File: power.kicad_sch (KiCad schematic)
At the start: 50 parts, among them SW2 SW_DPST, U10 ZLDO1117G33TA

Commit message: prepare for fabrication
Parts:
- C103, C107, C109, C116, C117, C138, C151, C222, C223, C227, C24, C29, C37, C38, C40, C50, C64, C66, C67, C70, C71, C85, C91, C92, C95: LCSC (none) -> C344201; LCSC Part (none) -> C344201
- C20, C21: LCSC C24123 -> C77083; LCSC Part C28323 -> C77083
- TP2, TP3: now not fitted
- U10: LCSC Part (none) -> C18212698

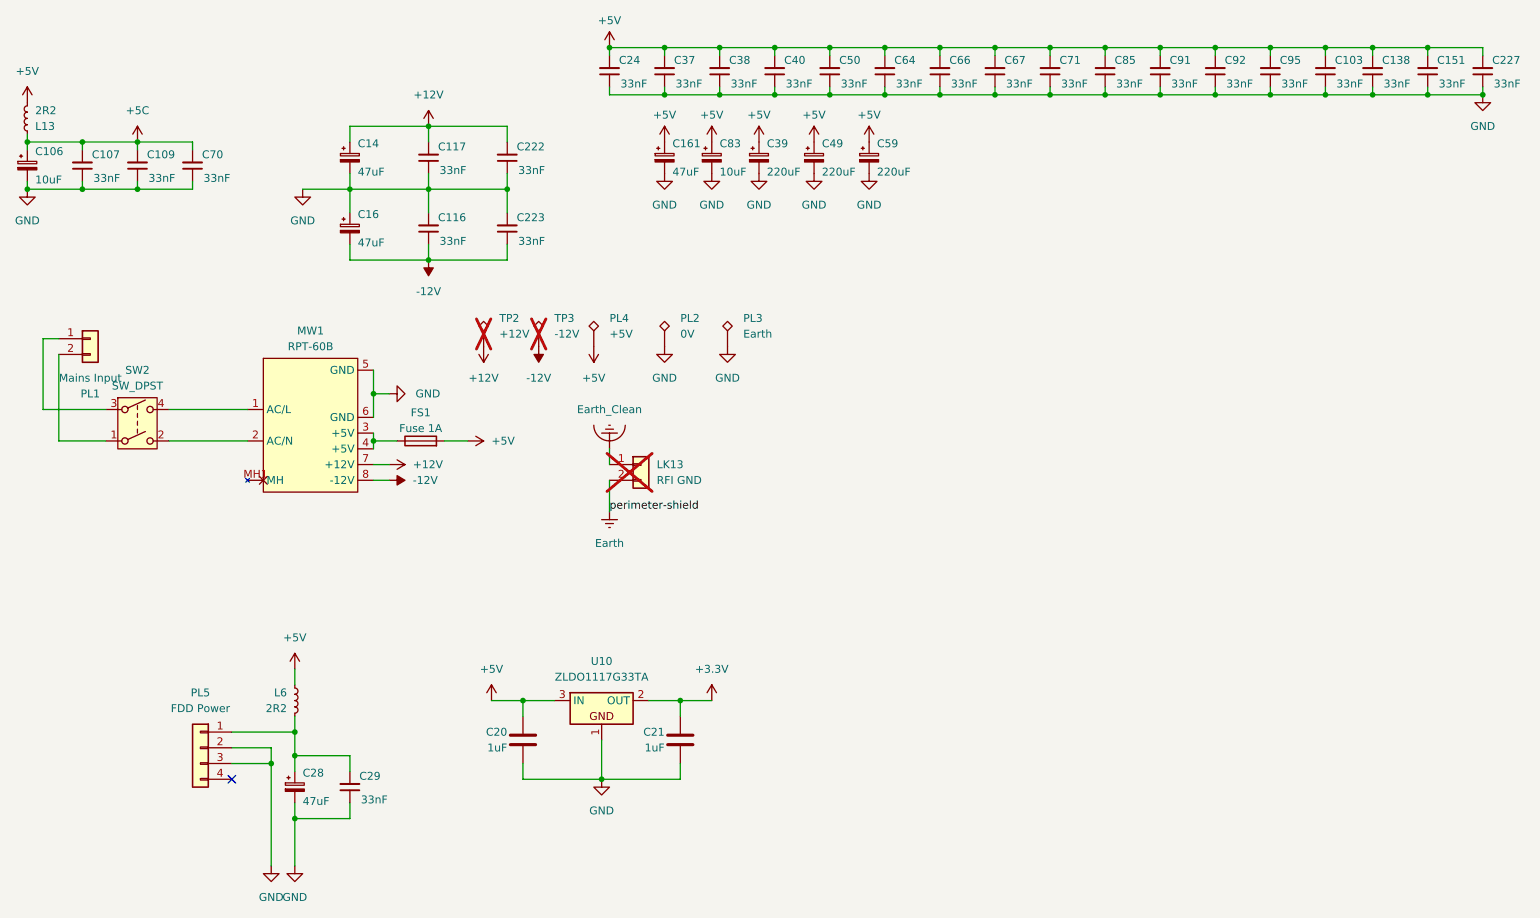
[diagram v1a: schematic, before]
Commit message: verify all component values vs TRM
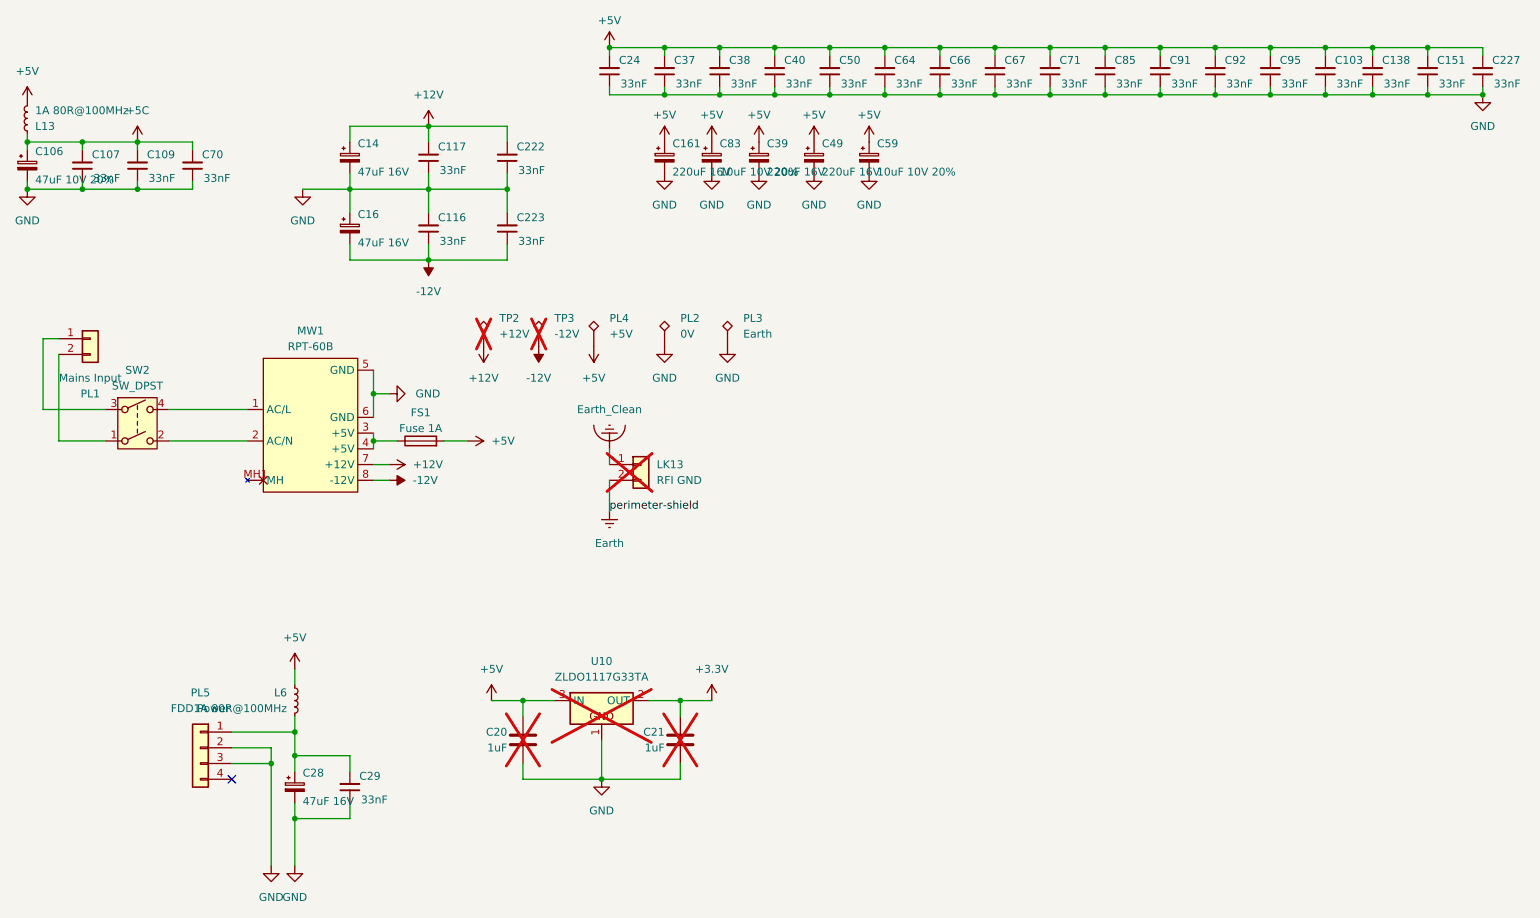
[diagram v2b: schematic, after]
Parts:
- C106: value 10uF -> 47uF 10V 20%
- C14, C16, C28: value 47uF -> 47uF 16V
- C161: value 47uF -> 220uF 16V
- C20, C21, U10: now not fitted; now left out of the parts list
- C39, C49: value 220uF -> 220uF 16V
- C59: value 220uF -> 10uF 10V 20%
- C83: value 10uF -> 10uF 10V 20%
- L13, L6: value 2R2 -> 1A 80R@100MHz
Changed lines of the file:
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@@
 			)
 		)
-		(property "Value" "220uF"
+		(property "Value" "220uF 16V"
 			(at 149.86 41.656 0)
 			(effects
@@
 			)
 		)
-		(property "Value" "47uF"
+		(property "Value" "220uF 16V"
 			(at 134.62 41.656 0)
 			(effects
@@
 			)
 		)
-		(property "Value" "220uF"
+		(property "Value" "10uF 10V 20%"
 			(at 167.64 41.656 0)
 			(effects
@@
 			)
 		)
-		(property "Value" "47uF"
+		(property "Value" "47uF 16V"
 			(at 83.82 41.656 0)
 			(effects
@@
 			)
 		)
-		(property "Value" "10uF"
+		(property "Value" "10uF 10V 20%"
 			(at 142.24 41.656 0)
 			(effects
@@
 		(unit 1)
 		(exclude_from_sim no)
-		(in_bom yes)
+		(in_bom no)
 		(on_board no)
-		(dnp no)
+		(dnp yes)
 		(fields_autoplaced yes)
 		(property "Reference" "U10"
@@
 		(unit 1)
 		(exclude_from_sim no)
-		(in_bom yes)
+		(in_bom no)
 		(on_board no)
-		(dnp no)
+		(dnp yes)
 		(property "Reference" "C21"
 			(at 133.35 132.08 0)
@@
 			)
 		)
-		(property "Value" "10uF"
+		(property "Value" "47uF 10V 20%"
 			(at 31.75 42.926 0)
 			(effects
@@
 		(unit 1)
 		(exclude_from_sim no)
-		(in_bom yes)
+		(in_bom no)
 		(on_board no)
-		(dnp no)
+		(dnp yes)
 		(property "Reference" "C20"
 			(at 107.95 132.08 0)
@@
 			)
 		)
-		(property "Value" "2R2"
+		(property "Value" "1A 80R@100MHz"
 			(at 72.39 128.2699 0)
 			(effects
@@
 			)
 		)
-		(property "Value" "47uF"
+		(property "Value" "47uF 16V"
 			(at 74.93 143.256 0)
 			(effects
@@
 			)
 		)
-		(property "Value" "220uF"
+		(property "Value" "220uF 16V"
 			(at 158.75 41.656 0)
 			(effects
@@
 			)
 		)
-		(property "Value" "2R2"
+		(property "Value" "1A 80R@100MHz"
 			(at 31.75 31.7501 0)
 			(effects
@@
 			)
 		)
-		(property "Value" "47uF"
+		(property "Value" "47uF 16V"
 			(at 83.82 53.086 0)
 			(effects

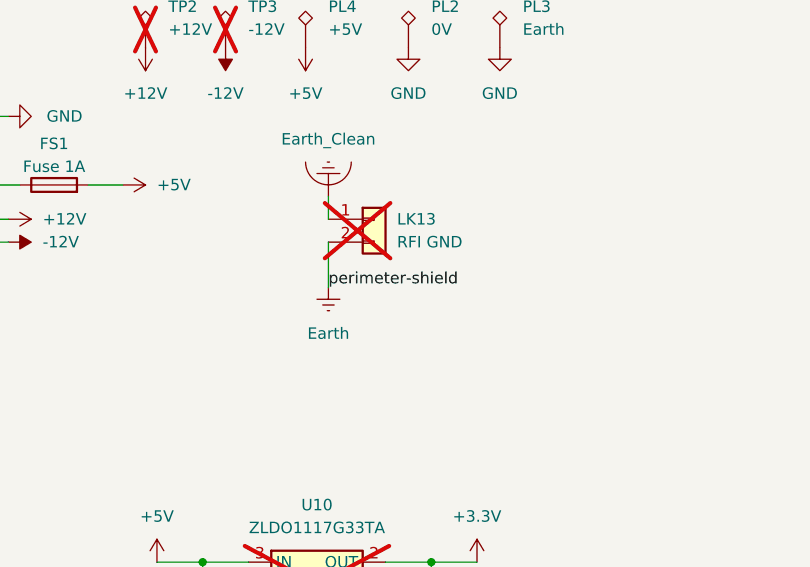
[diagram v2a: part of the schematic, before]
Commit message: switch links to net ties
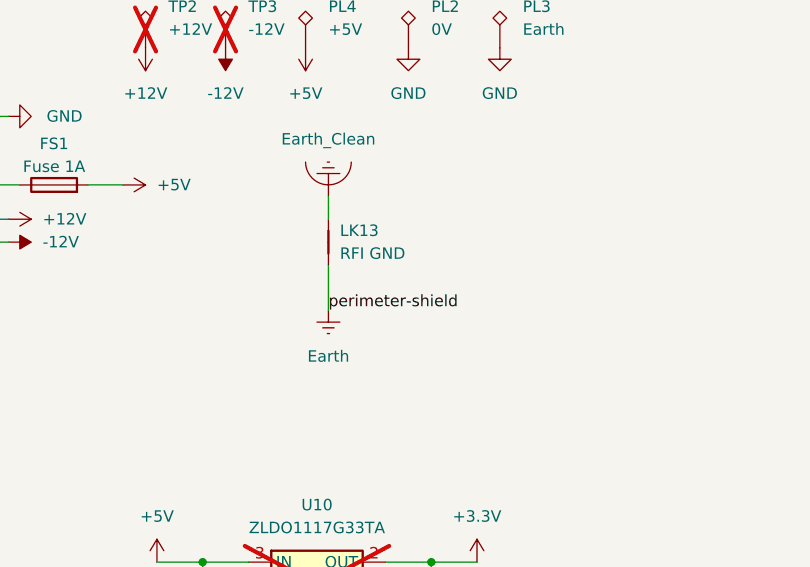
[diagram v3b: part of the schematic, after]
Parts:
- removed LK13: RFI GND, Connector_PinHeader_2.54mm:PinHeader_1x02_P2.54mm_Vertical, symbol Connector_Generic:Conn_01x02
- added LK13: RFI GND, Acorn:Link_Connected, symbol Device:NetTie_2
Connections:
- net Earth: now also LK13.1
- net Earth_Clean: now also LK13.2
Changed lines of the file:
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@@
 	(wire
 		(pts
-			(xy 124.46 91.44) (xy 124.46 96.52)
+			(xy 124.46 93.98) (xy 124.46 99.06)
 		)
 		(stroke
@@
 	)
 	(label "perimeter-shield"
-		(at 124.46 96.52 0)
+		(at 124.46 99.06 0)
 		(effects
 			(font
@@
 	)
 	(symbol
+		(lib_id "Device:NetTie_2")
+		(at 124.46 91.44 90)
+		(unit 1)
+		(exclude_from_sim no)
+		(in_bom no)
+		(on_board yes)
+		(dnp no)
+		(fields_autoplaced yes)
+		(property "Reference" "LK13"
+			(at 125.73 90.1699 90)
+			(effects
+				(font
+					(size 1.27 1.27)
+				)
+				(justify right)
+			)
+		)
+		(property "Value" "RFI GND"
+			(at 125.73 92.7099 90)
+			(effects
+				(font
+					(size 1.27 1.27)
+				)
+				(justify right)
+			)
+		)
+		(property "Footprint" "Acorn:Link_Connected"
+			(at 124.46 91.44 0)
+			(effects
+				(font
+					(size 1.27 1.27)
+				)
+				(hide yes)
+			)
+		)
+		(property "Datasheet" "~"
+			(at 124.46 91.44 0)
+			(effects
+				(font
+					(size 1.27 1.27)
+				)
+				(hide yes)
+			)
+		)
+		(property "Description" "Net tie, 2 pins"
+			(at 124.46 91.44 0)
+			(effects
+				(font
+					(size 1.27 1.27)
+				)
+				(hide yes)
+			)
+		)
+		(pin "1"
+		)
+		(pin "2"
+		)
+		(instances
+			(project "Acorn-A3010"
+				(path "/999882f3-94f8-4a89-9093-27a47d0cb289/5e8722fb-7afe-44d4-8a36-2936df1b76c5"
+					(reference "LK13")
+					(unit 1)
+				)
+			)
+		)
+	)
+	(symbol
 		(lib_id "Connector_Generic:Conn_01x02")
 		(at 40.64 68.58 0)
@@
 	(symbol
 		(lib_id "power:Earth")
-		(at 124.46 96.52 0)
+		(at 124.46 99.06 0)
 		(unit 1)
 		(exclude_from_sim no)
@@
 		(fields_autoplaced yes)
 		(property "Reference" "#PWR0310"
-			(at 124.46 102.87 0)
+			(at 124.46 105.41 0)
 			(effects
 				(font
@@
 		)
 		(property "Value" "Earth"
-			(at 124.46 101.6 0)
+			(at 124.46 104.14 0)
 			(effects
 				(font
@@
 		)
 		(property "Footprint" ""
-			(at 124.46 96.52 0)
+			(at 124.46 99.06 0)
 			(effects
 				(font
@@
 		)
 		(property "Datasheet" "~"
-			(at 124.46 96.52 0)
+			(at 124.46 99.06 0)
 			(effects
 				(font
@@
 		)
 		(property "Description" "Power symbol creates a global label with name \"Earth\""
-			(at 124.46 96.52 0)
+			(at 124.46 99.06 0)
 			(effects
 				(font
@@
 					(unit 1)
 				)
-			)
-		)
-	)
-	(symbol
-		(lib_id "Connector_Generic:Conn_01x02")
-		(at 129.54 88.9 0)
-		(unit 1)
-		(exclude_from_sim no)
-		(in_bom yes)
-		(on_board yes)
-		(dnp yes)
-		(fields_autoplaced yes)
-		(property "Reference" "LK13"
-			(at 132.08 88.8999 0)
-			(effects
-				(font
-					(size 1.27 1.27)
-				)
-				(justify left)
-			)
-		)
-		(property "Value" "RFI GND"
-			(at 132.08 91.4399 0)
-			(effects
-				(font
-					(size 1.27 1.27)
-				)
-				(justify left)
-			)
-		)
-		(property "Footprint" "Connector_PinHeader_2.54mm:PinHeader_1x02_P2.54mm_Vertical"
-			(at 129.54 88.9 0)
-			(effects
-				(font
-					(size 1.27 1.27)
-				)
-				(hide yes)
-			)
-		)
-		(property "Datasheet" "~"
-			(at 129.54 88.9 0)
-			(effects
-				(font
-					(size 1.27 1.27)
-				)
-				(hide yes)
-			)
-		)
-		(property "Description" "Generic connector, single row, 01x02, script generated (kicad-library-utils/schlib/autogen/connector/)"
-			(at 129.54 88.9 0)
-			(effects
-				(font
-					(size 1.27 1.27)
-				)
-				(hide yes)
-			)
-		)
-		(pin "1"
-		)
-		(pin "2"
-		)
-		(instances
-			(project "Acorn-A3010"
-				(path "/999882f3-94f8-4a89-9093-27a47d0cb289/5e8722fb-7afe-44d4-8a36-2936df1b76c5"
-					(reference "LK13")
-					(unit 1)
-				)

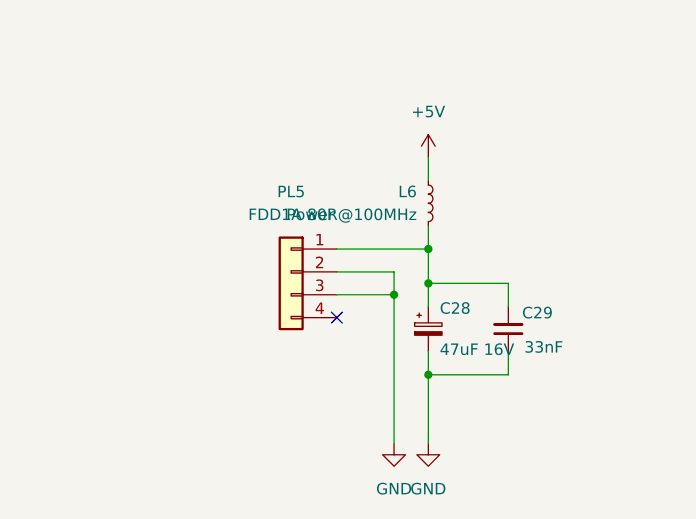
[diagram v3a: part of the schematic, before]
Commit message: fix power domain links with net ties
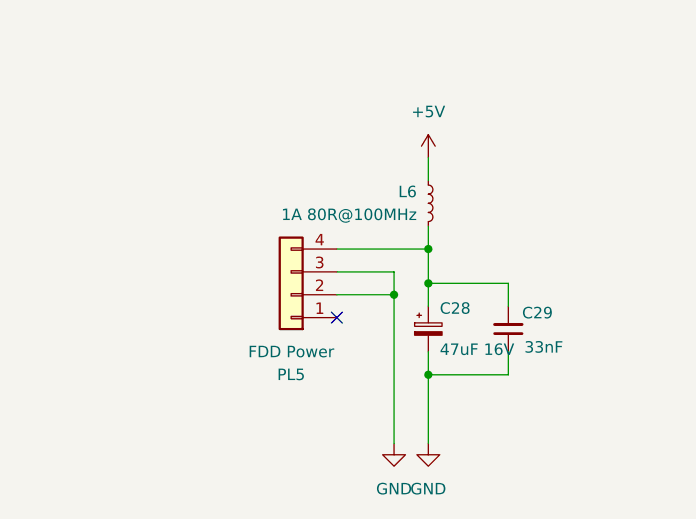
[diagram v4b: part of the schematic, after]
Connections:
- net at C28.1, C29.2, L6.2: now also PL5.4 (Pin_4); no longer PL5.1 (Pin_1)
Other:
- moved on the sheet: PL5
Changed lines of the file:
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@@
 	(symbol
 		(lib_id "Connector_Generic:Conn_01x04")
-		(at 58.42 134.62 0)
-		(mirror y)
+		(at 58.42 137.16 180)
 		(unit 1)
 		(exclude_from_sim no)
@@
 		(on_board yes)
 		(dnp no)
-		(fields_autoplaced yes)
 		(property "Reference" "PL5"
-			(at 58.42 125.73 0)
+			(at 58.42 146.05 0)
 			(effects
 				(font
@@
 		)
 		(property "Value" "FDD Power"
-			(at 58.42 128.27 0)
+			(at 58.42 143.51 0)
 			(effects
 				(font
@@
 		)
 		(property "Footprint" "Connector_Molex:Molex_KK-254_AE-6410-04A_1x04_P2.54mm_Vertical"
-			(at 58.42 134.62 0)
+			(at 58.42 137.16 0)
 			(effects
 				(font
@@
 		)
 		(property "Datasheet" "~"
-			(at 58.42 134.62 0)
+			(at 58.42 137.16 0)
 			(effects
 				(font
@@
 		)
 		(property "Description" "Generic connector, single row, 01x04, script generated (kicad-library-utils/schlib/autogen/connector/)"
-			(at 58.42 134.62 0)
+			(at 58.42 137.16 0)
 			(effects
 				(font

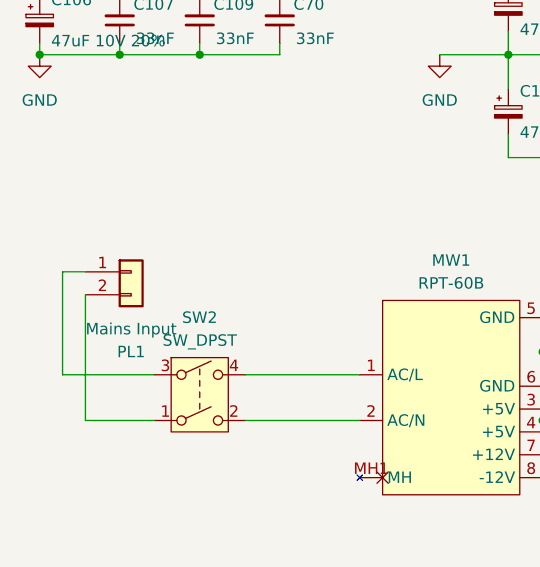
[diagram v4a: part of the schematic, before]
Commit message: fix power and cmposite output
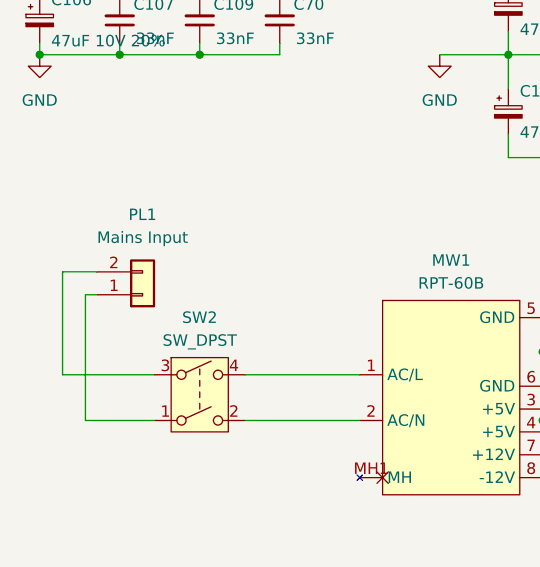
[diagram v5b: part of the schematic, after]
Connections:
- net at PL1.1 (Pin_1): now also SW2.1; no longer SW2.3
- net at PL1.2 (Pin_2): now also SW2.3; no longer SW2.1
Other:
- moved on the sheet: PL1
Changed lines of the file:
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@@
 	(wire
 		(pts
+			(xy 35.56 71.12) (xy 36.83 71.12)
+		)
+		(stroke
+			(width 0)
+			(type default)
+		)
+	)
+	(wire
+		(pts
 			(xy 124.46 27.94) (xy 124.46 29.21)
 		)
@@
 	(wire
 		(pts
-			(xy 35.56 68.58) (xy 33.02 68.58)
+			(xy 36.83 68.58) (xy 33.02 68.58)
 		)
 		(stroke
@@
 	(symbol
 		(lib_id "Connector_Generic:Conn_01x02")
-		(at 40.64 68.58 0)
+		(at 41.91 71.12 0)
+		(mirror x)
 		(unit 1)
 		(exclude_from_sim no)
@@
 		(dnp no)
 		(property "Reference" "PL1"
-			(at 40.64 77.47 0)
+			(at 41.91 62.23 0)
 			(effects
 				(font
@@
 		)
 		(property "Value" "Mains Input"
-			(at 40.64 74.93 0)
+			(at 41.91 64.77 0)
 			(effects
 				(font
@@
 		)
 		(property "Footprint" "Acorn:AC_Power_Header"
-			(at 40.64 68.58 0)
+			(at 41.91 71.12 0)
 			(effects
 				(font
@@
 		)
 		(property "Datasheet" "~"
-			(at 40.64 68.58 0)
+			(at 41.91 71.12 0)
 			(effects
 				(font
@@
 		)
 		(property "Description" "Generic connector, single row, 01x02, script generated (kicad-library-utils/schlib/autogen/connector/)"
-			(at 40.64 68.58 0)
+			(at 41.91 71.12 0)
 			(effects
 				(font

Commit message: V0.3 fabrication
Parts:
- MW1: footprint Acorn:RPT-60 -> Acorn:RPT-60_cutout
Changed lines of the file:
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@@
 			)
 		)
-		(property "Footprint" "Acorn:RPT-60"
+		(property "Footprint" "Acorn:RPT-60_cutout"
 			(at 76.2 82.55 0)
 			(effects

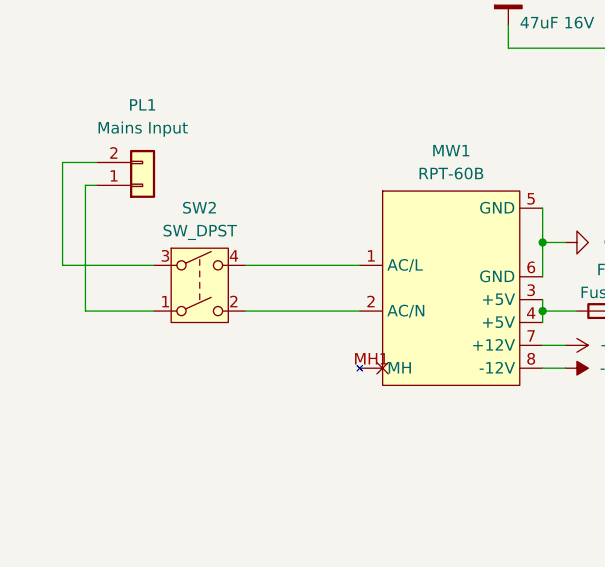
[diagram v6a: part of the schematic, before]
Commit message: fix mains power routing
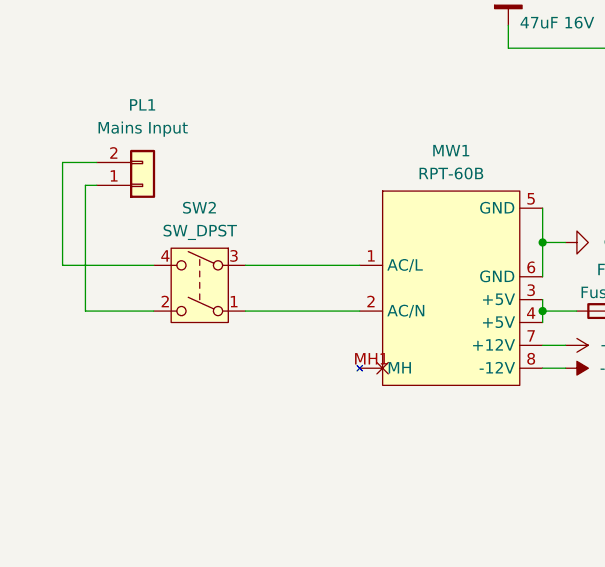
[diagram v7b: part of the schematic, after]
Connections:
- net at MW1.1 (AC/L): now also SW2.3; no longer SW2.4
- net at MW1.2 (AC/N): now also SW2.1; no longer SW2.2
- net at PL1.1 (Pin_1): now also SW2.2; no longer SW2.1
- net at PL1.2 (Pin_2): now also SW2.4; no longer SW2.3
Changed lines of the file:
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@@
 		(lib_id "Switch:SW_DPST")
 		(at 48.26 82.55 0)
+		(mirror y)
 		(unit 1)
 		(exclude_from_sim no)
@@
 		(on_board yes)
 		(dnp no)
-		(fields_autoplaced yes)
 		(property "Reference" "SW2"
 			(at 48.26 73.66 0)

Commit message: enforce net class on AC
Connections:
- net AC_SW_L: now reaches MW1.1 (AC/L), SW2.3
- net AC_SW_N: now reaches MW1.2 (AC/N), SW2.1
- net AC_N: now reaches PL1.1 (Pin_1), SW2.2
- net AC_L: now reaches PL1.2 (Pin_2), SW2.4
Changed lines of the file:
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@@
+		)
+	)
+	(label "AC_SW_L"
+		(at 54.61 80.01 0)
+		(effects
+			(font
+				(size 1.27 1.27)
+			)
+			(justify left bottom)
+		)
+	)
+	(label "AC_SW_N"
+		(at 54.61 85.09 0)
+		(effects
+			(font
+				(size 1.27 1.27)
+			)
+			(justify left bottom)
 		)
 	)
@@
 		(effects
 			(font
+				(size 1.27 1.27)
+			)
+			(justify left bottom)
+		)
+	)
+	(label "AC_L"
+		(at 36.83 80.01 0)
+		(effects
+			(font
+				(size 1.27 1.27)
+			)
+			(justify left bottom)
+		)
+	)
+	(label "AC_N"
+		(at 36.83 85.09 0)
+		(effects
+			(font
